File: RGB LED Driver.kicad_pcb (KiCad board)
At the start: 2 copper layers, 97.5 x 79 mm, 140 parts, among them J1 USB4085, J2 Conn_01x06_Pin, Q1 AO3400A, Q2 AO3400A, Q3 AO3400A, Q4 AO3400A, SW1 BOOT, U1 TPS61170DRVR, U10 LM358, U2 AP2112K-3.3TRG1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

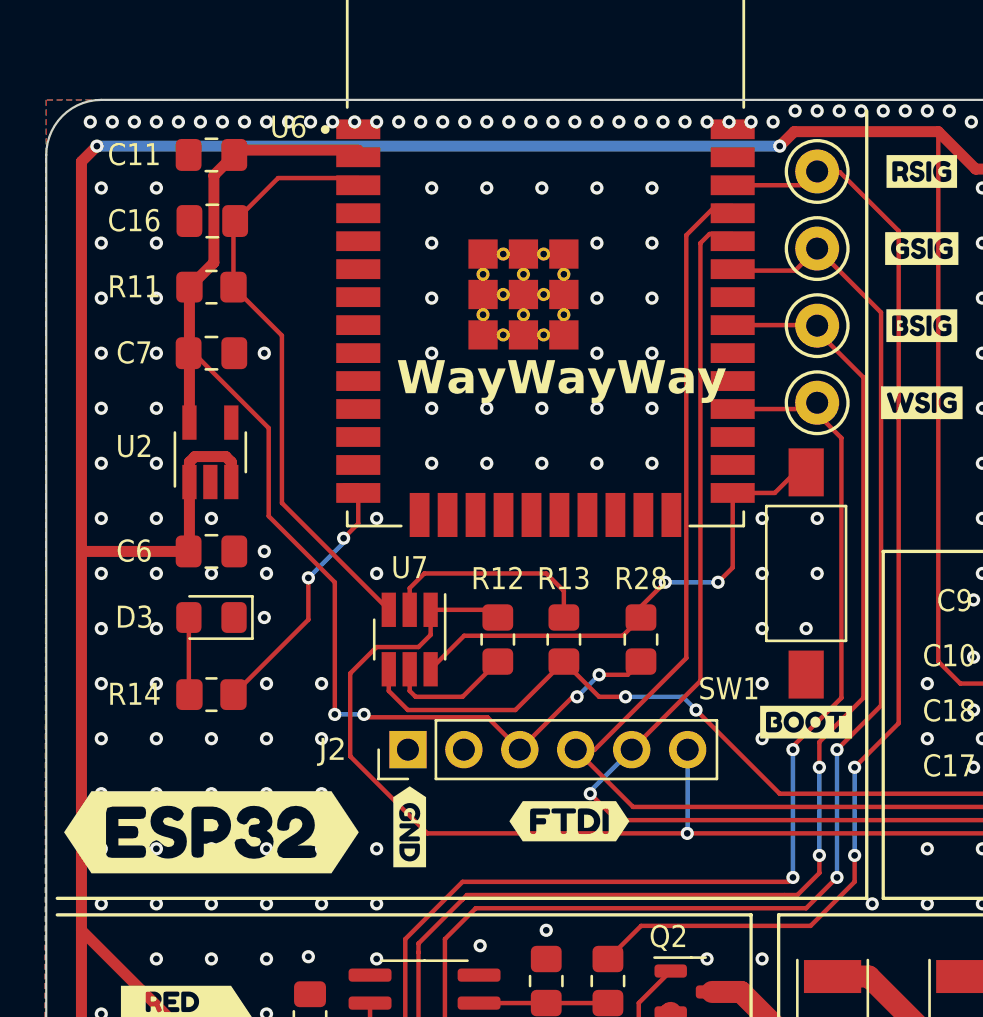
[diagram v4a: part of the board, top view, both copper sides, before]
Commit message: added jumper to FTDI power
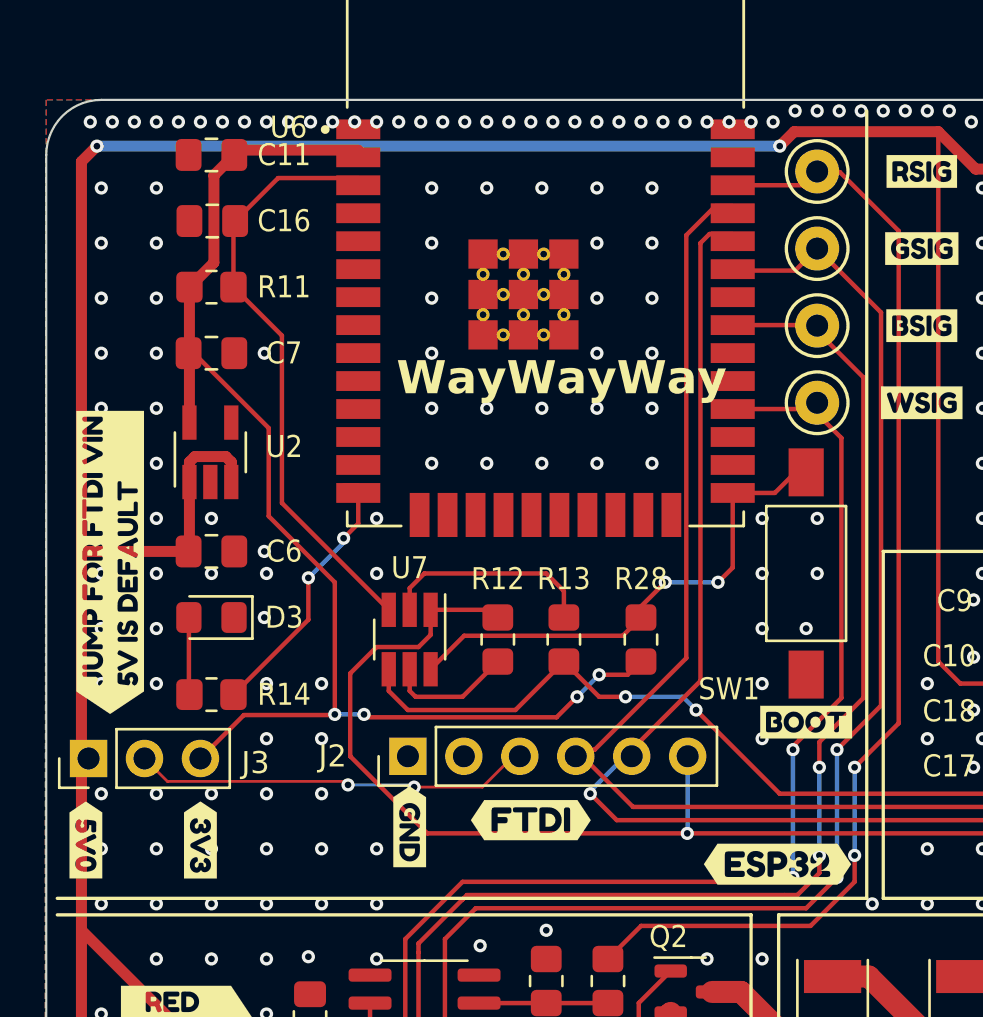
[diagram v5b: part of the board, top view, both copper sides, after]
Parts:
- removed kibuzzard-65932565: G***, kibuzzard-65932565
- added J3: Conn_01x03_Pin, Connector_PinHeader_2.54mm:PinHeader_1x03_P2.54mm_Vertical, F.Cu at (84.4, 83.4)
- added kibuzzard-6594327C: G***, kibuzzard-6594327C, F.Cu at (115.7, 88.2)
- added kibuzzard-65943322: G***, kibuzzard-65943322, F.Cu at (84.3, 87.1)
- added kibuzzard-6594332E: G***, kibuzzard-6594332E, F.Cu at (89.5, 87.1)
- added kibuzzard-659433EE: G***, kibuzzard-659433EE, F.Cu at (85.4, 74.5)
- moved kibuzzard-65932434 1.75 mm to (104.5, 86.2)
- moved J2 0.30 mm to (98.9, 83.3)
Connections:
- J2 pad 3: +3.3V -> /ESP32/FTDI_VIN
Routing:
- net /ESP32/FTDI_VIN: track 0.00 -> 18.3 mm, vias 0 -> 2
- net +3.3V: track 54.3 -> 60.2 mm
- net GND: vias 701 -> 698

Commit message: [A02] Edited resistor values
R11 to 51K to allow for auto reset
R3 to 270K for 34V output
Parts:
- R11: value 10K -> 51K
- R3: value 300K -> 270K
- R4: value 10K/1% -> 10K
- U5: value CP2104-F03-GM -> CP2102N-A02-GQFN24
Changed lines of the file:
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@@
   (title_block
     (title "RGB LED Driver Demo Board")
-    (date "2024-01-01")
-    (rev "A01")
+    (date "2024-01-17")
+    (rev "A02")
     (company "The Art and Science of PCB Design")
   )
@@
     (tags "resistor handsolder")
     (property "Digikey PN" "RMCF0805FT51K0CT-ND")
-    (property "MPN" "RMCF0805FT51K0")
+    (property "MPN" "RMCF0805FT10K0")
     (property "Sheetfile" "led_driver.kicad_sch")
     (property "Sheetname" "LED Driver B")
@@
     (descr "Capacitor SMD 0805 (2012 Metric), square (rectangular) end terminal, IPC_7351 nominal with elongated pad for handsoldering. (Body size source: IPC-SM-782 page 76, https://www.pcb-3d.com/wordpress/wp-content/uploads/ipc-sm-782a_amendment_1_and_2.pdf, https://docs.google.com/spreadsheets/d/1BsfQQcO9C6DZCsRaXUlFlo91Tg2WpOkGARC1WS5S8t0/edit?usp=sharing), generated with kicad-footprint-generator")
     (tags "capacitor handsolder")
-    (property "Digikey PN" "1276-1003-1-ND")
-    (property "MPN" "CL21B104KBCNNNC")
+    (property "Digikey PN" "1276-1029-1-ND")
+    (property "MPN" "CL21B105KBFNNNE")
     (property "Sheetfile" "usb_serial.kicad_sch")
     (property "Sheetname" "USB-Serial")
@@
     (descr "Capacitor SMD 0805 (2012 Metric), square (rectangular) end terminal, IPC_7351 nominal with elongated pad for handsoldering. (Body size source: IPC-SM-782 page 76, https://www.pcb-3d.com/wordpress/wp-content/uploads/ipc-sm-782a_amendment_1_and_2.pdf, https://docs.google.com/spreadsheets/d/1BsfQQcO9C6DZCsRaXUlFlo91Tg2WpOkGARC1WS5S8t0/edit?usp=sharing), generated with kicad-footprint-generator")
     (tags "capacitor handsolder")
-    (property "Digikey PN" "399-C0805C153G5GEC7800CT-ND")
-    (property "MPN" "C0805C153G5GEC7800")
+    (property "Digikey PN" "399-C0805C153K5RAC7800CT-ND")
+    (property "MPN" "C0805C153K5RAC7800")
     (property "Sheetfile" "boost_converter.kicad_sch")
     (property "Sheetname" "Boost_Converter")
@@
     (tags "QFN NoLead")
     (property "Digikey PN" "336-4146-1-ND")
-    (property "MPN" "CP2104-F03-GM")
+    (property "MPN" "CP2102N-A02-GQFN24")
     (property "Sheetfile" "usb_serial.kicad_sch")
     (property "Sheetname" "USB-Serial")
@@
         (effects (font (size 1 0.9) (thickness 0.15)))
     )
-    (fp_text value "CP2104-F03-GM" (at 0 3.3 -270) (layer "F.Fab") hide
+    (fp_text value "CP2102N-A02-GQFN24" (at 0 3.3 -270) (layer "F.Fab") hide
         (effects (font (size 1 0.9) (thickness 0.15)))
     )
@@
     (descr "Capacitor SMD 0805 (2012 Metric), square (rectangular) end terminal, IPC_7351 nominal with elongated pad for handsoldering. (Body size source: IPC-SM-782 page 76, https://www.pcb-3d.com/wordpress/wp-content/uploads/ipc-sm-782a_amendment_1_and_2.pdf, https://docs.google.com/spreadsheets/d/1BsfQQcO9C6DZCsRaXUlFlo91Tg2WpOkGARC1WS5S8t0/edit?usp=sharing), generated with kicad-footprint-generator")
     (tags "capacitor handsolder")
-    (property "Digikey PN" "1276-1003-1-ND")
-    (property "MPN" "CL21B104KBCNNNC")
+    (property "Digikey PN" "1276-1029-1-ND")
+    (property "MPN" "CL21B105KBFNNNE")
     (property "Sheetfile" "esp32.kicad_sch")
     (property "Sheetname" "ESP32")
@@
         (effects (font (size 1 0.9) (thickness 0.15)))
     )
-    (fp_text value "300K" (at 0 1.65) (layer "F.Fab") hide
+    (fp_text value "270K" (at 0 1.65) (layer "F.Fab") hide
         (effects (font (size 1 0.9) (thickness 0.15)))
     )
@@
     (descr "Through hole straight pin header, 1x06, 2.54mm pitch, single row")
     (tags "Through hole pin header THT 1x06 2.54mm single row")
-    (property "Digikey PN" "")
+    (property "Digikey PN" "2057-PH1-06-UA-ND")
+    (property "MPN" "PH1-06-UA")
     (property "Sheetfile" "esp32.kicad_sch")
     (property "Sheetname" "ESP32")
@@
     (tags "resistor handsolder")
     (property "Digikey PN" "RMCF0805FT51K0CT-ND")
-    (property "MPN" "RMCF0805FT51K0")
+    (property "MPN" "RMCF0805FT10K0")
     (property "Sheetfile" "led_driver.kicad_sch")
     (property "Sheetname" "LED Driver W")
@@
     (descr "Through hole straight pin header, 1x03, 2.54mm pitch, single row")
     (tags "Through hole pin header THT 1x03 2.54mm single row")
+    (property "Digikey PN" "2057-PH1-03-UA-ND")
+    (property "MPN" "PH1-03-UA")
     (property "Sheetfile" "esp32.kicad_sch")
     (property "Sheetname" "ESP32")
@@
     (descr "Capacitor SMD 0805 (2012 Metric), square (rectangular) end terminal, IPC_7351 nominal with elongated pad for handsoldering. (Body size source: IPC-SM-782 page 76, https://www.pcb-3d.com/wordpress/wp-content/uploads/ipc-sm-782a_amendment_1_and_2.pdf, https://docs.google.com/spreadsheets/d/1BsfQQcO9C6DZCsRaXUlFlo91Tg2WpOkGARC1WS5S8t0/edit?usp=sharing), generated with kicad-footprint-generator")
     (tags "capacitor handsolder")
-    (property "Digikey PN" "1276-1003-1-ND")
-    (property "MPN" "CL21B104KBCNNNC")
+    (property "Digikey PN" "1276-1029-1-ND")
+    (property "MPN" "CL21B105KBFNNNE")
     (property "Sheetfile" "boost_converter.kicad_sch")
     (property "Sheetname" "Boost_Converter")
@@
     (tags "resistor handsolder")
     (property "Digikey PN" "RMCF0805FT51K0CT-ND")
-    (property "MPN" "RMCF0805FT51K0")
+    (property "MPN" "RMCF0805FT10K0")
     (property "Sheetfile" "led_driver.kicad_sch")
     (property "Sheetname" "LED Driver R")
@@
     (descr "Resistor SMD 0805 (2012 Metric), square (rectangular) end terminal, IPC_7351 nominal with elongated pad for handsoldering. (Body size source: IPC-SM-782 page 72, https://www.pcb-3d.com/wordpress/wp-content/uploads/ipc-sm-782a_amendment_1_and_2.pdf), generated with kicad-footprint-generator")
     (tags "resistor handsolder")
-    (property "Digikey PN" "RMCF0805FT10K0CT-ND")
+    (property "Digikey PN" "RMCF0805FT51K0CT-ND")
     (property "MPN" "RMCF0805FT10K0")
     (property "Sheetfile" "esp32.kicad_sch")
@@
         (effects (font (size 1 0.9) (thickness 0.15)))
     )
-    (fp_text value "10K" (at 0 1.65) (layer "F.Fab") hide
+    (fp_text value "51K" (at 0 1.65) (layer "F.Fab") hide
         (effects (font (size 1 0.9) (thickness 0.15)))
     )
@@
     (descr "Capacitor SMD 0805 (2012 Metric), square (rectangular) end terminal, IPC_7351 nominal with elongated pad for handsoldering. (Body size source: IPC-SM-782 page 76, https://www.pcb-3d.com/wordpress/wp-content/uploads/ipc-sm-782a_amendment_1_and_2.pdf, https://docs.google.com/spreadsheets/d/1BsfQQcO9C6DZCsRaXUlFlo91Tg2WpOkGARC1WS5S8t0/edit?usp=sharing), generated with kicad-footprint-generator")
     (tags "capacitor handsolder")
-    (property "Digikey PN" "1276-1003-1-ND")
-    (property "MPN" "CL21B104KBCNNNC")
+    (property "Digikey PN" "1276-1029-1-ND")
+    (property "MPN" "CL21B105KBFNNNE")
     (property "Sheetfile" "usb_serial.kicad_sch")
     (property "Sheetname" "USB-Serial")
@@
     (tags "resistor handsolder")
     (property "Digikey PN" "RMCF0805FT51K0CT-ND")
-    (property "MPN" "RMCF0805FT51K0")
+    (property "MPN" "RMCF0805FT10K0")
     (property "Sheetfile" "led_driver.kicad_sch")
     (property "Sheetname" "LED Driver G")
@@
         (effects (font (size 1 0.9) (thickness 0.15)))
     )
-    (fp_text value "10K/1%" (at 0 1.65 90) (layer "F.Fab") hide
+    (fp_text value "10K" (at 0 1.65 90) (layer "F.Fab") hide
         (effects (font (size 1 0.9) (thickness 0.15)))
     )
@@
     (descr "Capacitor SMD 0805 (2012 Metric), square (rectangular) end terminal, IPC_7351 nominal with elongated pad for handsoldering. (Body size source: IPC-SM-782 page 76, https://www.pcb-3d.com/wordpress/wp-content/uploads/ipc-sm-782a_amendment_1_and_2.pdf, https://docs.google.com/spreadsheets/d/1BsfQQcO9C6DZCsRaXUlFlo91Tg2WpOkGARC1WS5S8t0/edit?usp=sharing), generated with kicad-footprint-generator")
     (tags "capacitor handsolder")
-    (property "Digikey PN" "1276-1003-1-ND")
-    (property "MPN" "CL21B104KBCNNNC")
+    (property "Digikey PN" "1276-1029-1-ND")
+    (property "MPN" "CL21B105KBFNNNE")
     (property "Sheetfile" "esp32.kicad_sch")
     (property "Sheetname" "ESP32")
